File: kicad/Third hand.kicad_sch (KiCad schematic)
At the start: 74 parts, among them Q301 DMN32D2, Q310 DMP2900, Q323 DMN32D2, Q332 DMP2900, Q345 DMN32D2, Q354 DMP2900, Q367 DMN32D2, Q389 DMN32D2, U301 74HC595, U302 74HC595

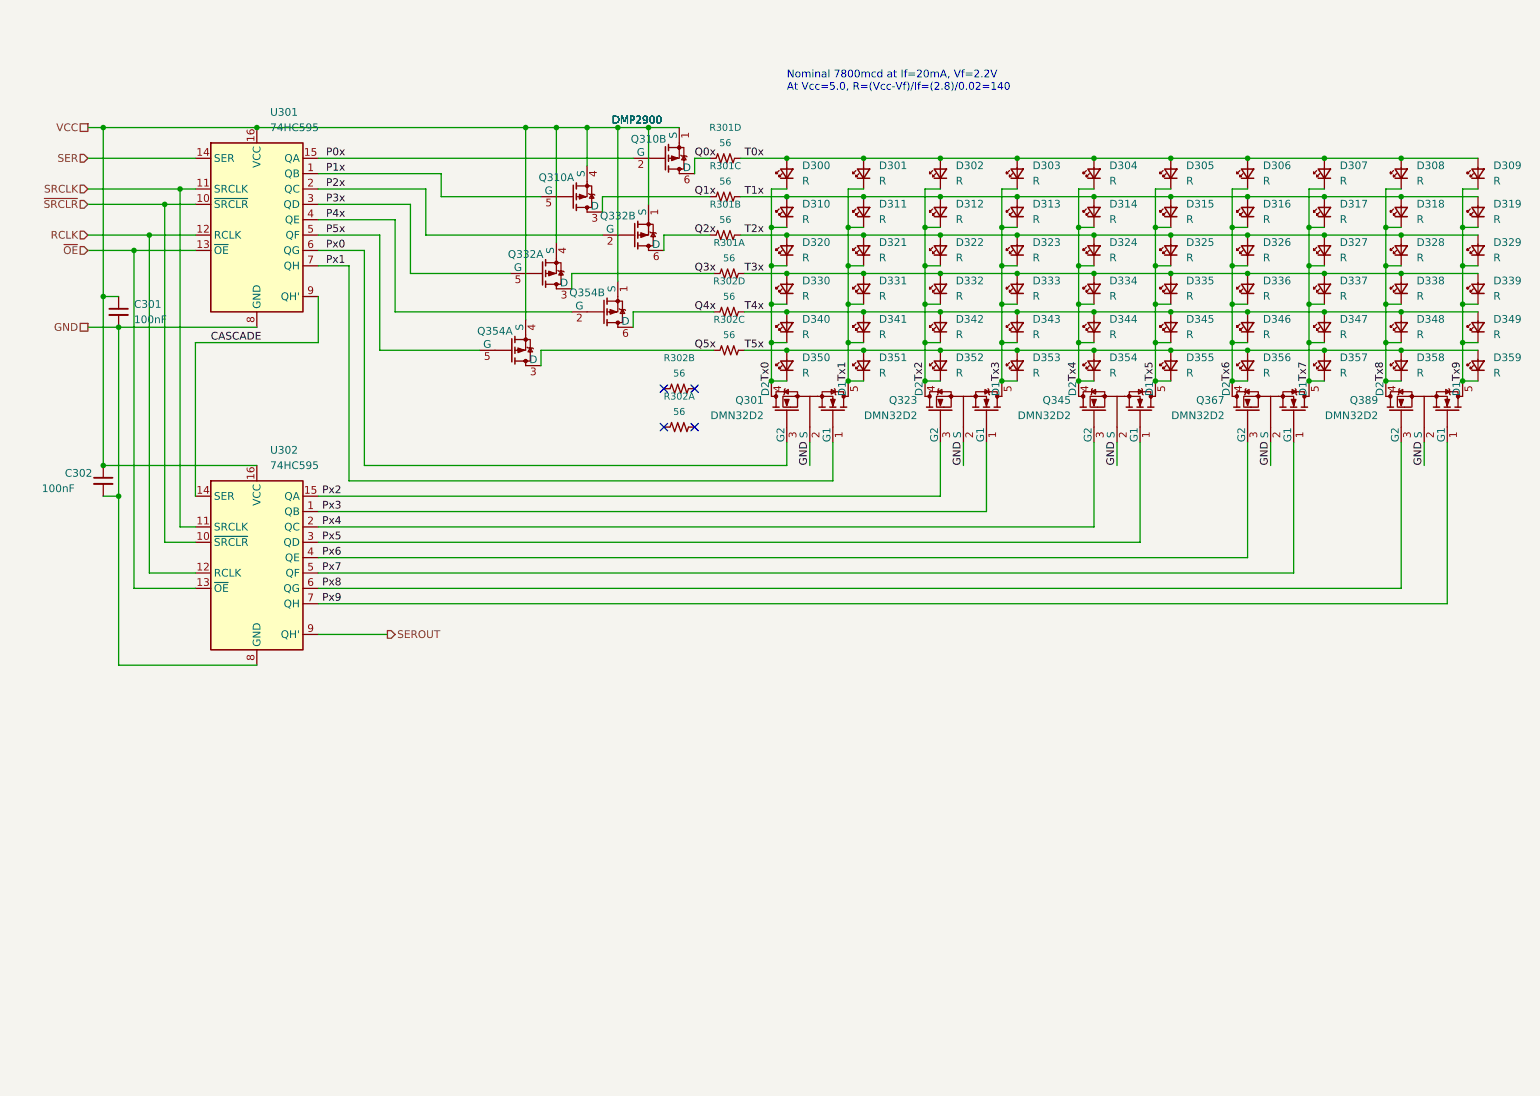
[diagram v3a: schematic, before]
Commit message: Continue wiring MOSFET switches
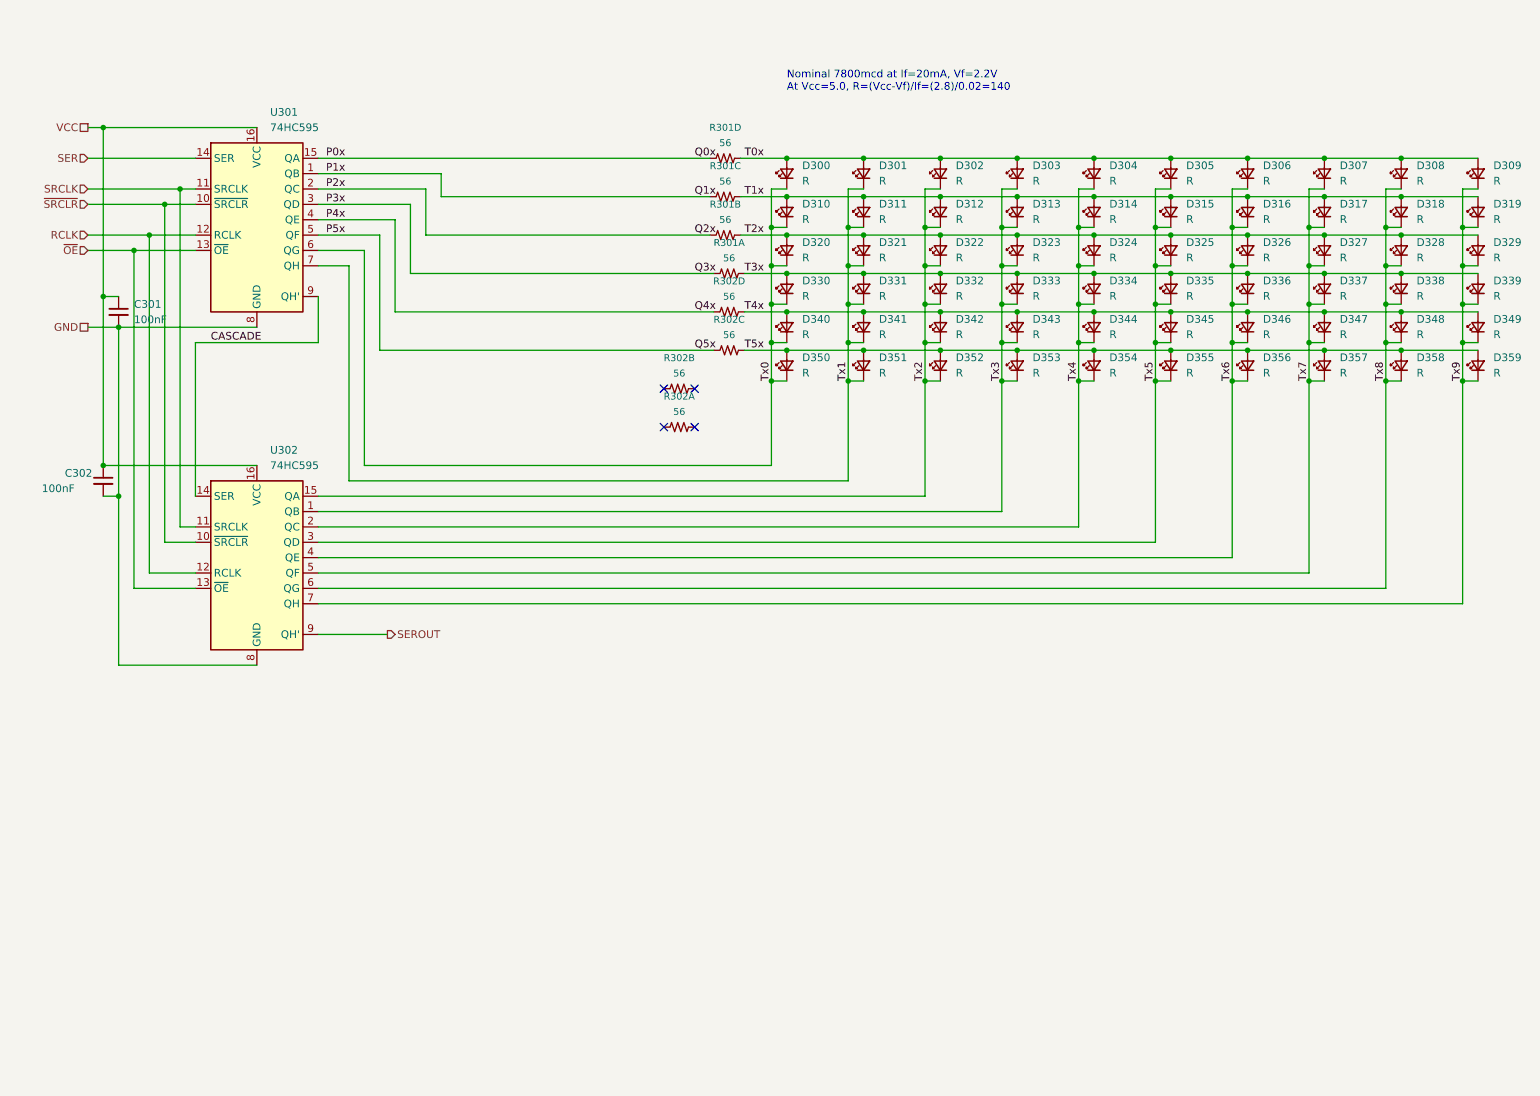
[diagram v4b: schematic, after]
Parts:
- removed Q301, Q323, Q345, Q367, Q389: DMN32D2, Package_TO_SOT_SMD:SOT-353_SC-70-5, symbol KwanSystems:NMOS_DUAL_COMMON_SOURCE
- removed Q310, Q332, Q354: DMP2900, Package_TO_SOT_SMD:SOT-363_SC-70-6, symbol KwanSystems:PMOS_DUAL
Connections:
- net Px0 is gone; now on net Tx0: U301.6 (QG)
- net Px1 is gone; now on net Tx1: U301.7 (QH)
- net Px2 is gone; now on net Tx2: U302.15 (QA)
- net Px3 is gone; now on net Tx3: U302.1 (QB)
- net Px4 is gone; now on net Tx4: U302.2 (QC)
- net Px5 is gone; now on net Tx5: U302.3 (QD)
- net Px6 is gone; now on net Tx6: U302.4 (QE)
- net Px7 is gone; now on net Tx7: U302.5 (QF)
- net Px8 is gone; now on net Tx8: U302.6 (QG)
- net Px9 is gone; now on net Tx9: U302.7 (QH)
- net Q0x is gone; now on net P0x: R301.4
- net Q1x is gone; now on net P1x: R301.3 (4)
- net Q2x is gone; now on net P2x: R301.2 (4)
- net Q3x is gone; now on net P3x: R301.1 (4)
- net Q4x is gone; now on net P4x: R302.4
- net Q5x is gone; now on net P5x: R302.3 (4)

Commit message: Matrix8x8 stuff
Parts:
- removed C301, C302: 100nF, Capacitor_SMD:C_0603_1608Metric, symbol Device:C_Small
- removed D300, D301, D302, D303, D304, D305, D306, D307, D308, D309, D310, D311, D312, D313, D314, D315, D316, D317, D318, D319, D320, D321, D322, D323, D324, D325, D326, D327, D328, D329, D330, D331, D332, D333, D334, D335, D336, D337, D338, D339, D340, D341, D342, D343, D344, D345, D346, D347, D348, D349, D350, D351, D352, D353, D354, D355, D356, D357, D358, D359: R, KwanSystems:D_KINGBRIGHT_DOME, symbol Device:LED_Small
- removed R301, R302: 56, KwanSystems:R_Array_Convex_4x0402, symbol KwanSystems:RP4
- removed U301, U302: 74HC595, Package_SO:TSSOP-16_4.4x5mm_P0.65mm, symbol 74xx:74HC595
- added C201 (x2), C202 (x2): 100nF, Capacitor_SMD:C_0603_1608Metric, symbol Device:C_Small
- added D200 (x2), D201 (x2), D202 (x2), D203 (x2), D204 (x2), D205 (x2), D206 (x2), D207 (x2), D208 (x2), D209 (x2), D210 (x2), D211 (x2), D212 (x2), D213 (x2), D214 (x2), D215 (x2), D216 (x2), D217 (x2), D218 (x2), D219 (x2), D220 (x2), D221 (x2), D222 (x2), D223 (x2), D224 (x2), D225 (x2), D226 (x2), D227 (x2), D228 (x2), D229 (x2), D230 (x2), D231 (x2), D232 (x2), D233 (x2), D234 (x2), D235 (x2), D236 (x2), D237 (x2), D238 (x2), D239 (x2), D240 (x2), D241 (x2), D242 (x2), D243 (x2), D244 (x2), D245 (x2), D246 (x2), D247 (x2), D248 (x2), D249 (x2), D250 (x2), D251 (x2), D252 (x2), D253 (x2), D254 (x2), D255 (x2), D256 (x2), D257 (x2), D258 (x2), D259 (x2): Y, KwanSystems:D_KINGBRIGHT_DOME, symbol Device:LED_Small
- added Q201 (x2), Q202 (x2), Q203 (x2), Q204 (x2): PMOS_DUAL, Package_TO_SOT_SMD:SOT-363_SC-70-6, symbol KwanSystems:PMOS_DUAL
- added R201 (x2): 1k, Resistor_SMD:R_0603_1608Metric, symbol KwanSystems:RESISTOR
- added U201 (x2): 74HC595, Package_SO:TSSOP-16_4.4x5mm_P0.65mm, symbol 74xx:74HC595
- added U202 (x2): STP08CP05, Package_SO:TSSOP-16_4.4x5mm_P0.65mm, symbol Driver_LED:STP08CP05
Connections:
- net CASCADE: now also U201.9 (QH'), U202.2 (SDI)
- net GND: now also C201.2, C202.2, R201.1, U201.13 (~{OE}), U201.8 (GND), U202.1 (GND)
- net P0x: now also Q201.5 (G), U201.15 (QA)
- net P1x: now also Q201.2 (G), U201.1 (QB)
- net P2x: now also Q202.5 (G), U201.2 (QC)
- net P3x: now also Q202.2 (G), U201.3 (QD)
- net P4x: now also Q203.5 (G), U201.4 (QE)
- net P5x: now also Q203.2 (G), U201.5 (QF)
- net RCLK: now also U201.12 (RCLK), U202.4 (LE)
- net SER: now also U201.14 (SER)
- net SEROUT: now also U202.14 (SDO)
- net SRCLK: now also U201.11 (SRCLK), U202.3 (CLK)
- net T0x: now also D200.2 (A), D201.2 (A), D202.2 (A), D203.2 (A), D204.2 (A), D205.2 (A), D206.2 (A), D207.2 (A), Q201.3 (D)
- net T1x: now also D208.2 (A), D209.2 (A), D210.2 (A), D211.2 (A), D212.2 (A), D213.2 (A), D214.2 (A), D215.2 (A), Q201.6 (D)
- net T2x: now also D216.2 (A), D217.2 (A), D218.2 (A), D219.2 (A), D220.2 (A), D221.2 (A), D222.2 (A), D223.2 (A), Q202.3 (D)
- net T3x: now also D224.2 (A), D225.2 (A), D226.2 (A), D227.2 (A), D228.2 (A), D229.2 (A), D230.2 (A), D231.2 (A), Q202.6 (D)
- net T4x: now also D232.2 (A), D233.2 (A), D234.2 (A), D235.2 (A), D236.2 (A), D237.2 (A), D238.2 (A), D239.2 (A), Q203.3 (D)
- net T5x: now also D240.2 (A), D241.2 (A), D242.2 (A), D243.2 (A), D244.2 (A), D245.2 (A), D246.2 (A), D247.2 (A), Q203.6 (D)
- net Tx0: now also D200.1 (K), D208.1 (K), D216.1 (K), D224.1 (K), D232.1 (K), D240.1 (K), D248.1 (K), D256.1 (K), U202.5 (OUT0)
- net Tx1: now also D201.1 (K), D209.1 (K), D217.1 (K), D225.1 (K), D233.1 (K), D241.1 (K), D249.1 (K), D257.1 (K), U202.6 (OUT1)
- net Tx2: now also D202.1 (K), D210.1 (K), D218.1 (K), D226.1 (K), D234.1 (K), D242.1 (K), D250.1 (K), D258.1 (K), U202.7 (OUT2)
- net Tx3: now also D203.1 (K), D211.1 (K), D219.1 (K), D227.1 (K), D235.1 (K), D243.1 (K), D251.1 (K), D259.1 (K), U202.8 (OUT3)
- net Tx4: now also D204.1 (K), D212.1 (K), D220.1 (K), D228.1 (K), D236.1 (K), D244.1 (K), D252.1 (K), U202.9 (OUT4)
- net Tx5: now also D205.1 (K), D213.1 (K), D221.1 (K), D229.1 (K), D237.1 (K), D245.1 (K), D253.1 (K), U202.10 (OUT5)
- net Tx6: now also D206.1 (K), D214.1 (K), D222.1 (K), D230.1 (K), D238.1 (K), D246.1 (K), D254.1 (K), U202.11 (OUT6)
- net Tx7: now also D207.1 (K), D215.1 (K), D223.1 (K), D231.1 (K), D239.1 (K), D247.1 (K), D255.1 (K), U202.12 (OUT7)
- net VCC: now also C201.1, C202.1, Q201.1 (S), Q201.4 (S), Q202.1 (S), Q202.4 (S), Q203.1 (S), Q203.4 (S), Q204.1 (S), Q204.4 (S), U201.10 (~{SRCLR}), U201.16 (VCC), U202.16 (VDD)
- net ~{OE}: now also U202.13 (~{OE})
- new net P6x: Q204.5 (G), U201.6 (QG)
- new net P7x: Q204.2 (G), U201.7 (QH)
- new net R_EXT: R201.2, U202.15 (R-EXT)
- new net T6x: D248.2 (A), D249.2 (A), D250.2 (A), D251.2 (A), D252.2 (A), D253.2 (A), D254.2 (A), D255.2 (A), Q204.3 (D)
- new net T7x: D256.2 (A), D257.2 (A), D258.2 (A), D259.2 (A), Q204.6 (D)
- no-connect marks 4 -> 182
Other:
- note added: "Rext (R) Iout (mA) 6740 3 3930 5 1913 10 963 20 386 50 241 80 124 130"
- note removed: "Nominal 7800mcd at If=20mA, Vf=2.2V At Vcc=5.0, R=(Vcc-Vf)/If=(2.8)/0.02=140"
